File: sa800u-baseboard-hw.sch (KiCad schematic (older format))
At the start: 4 parts

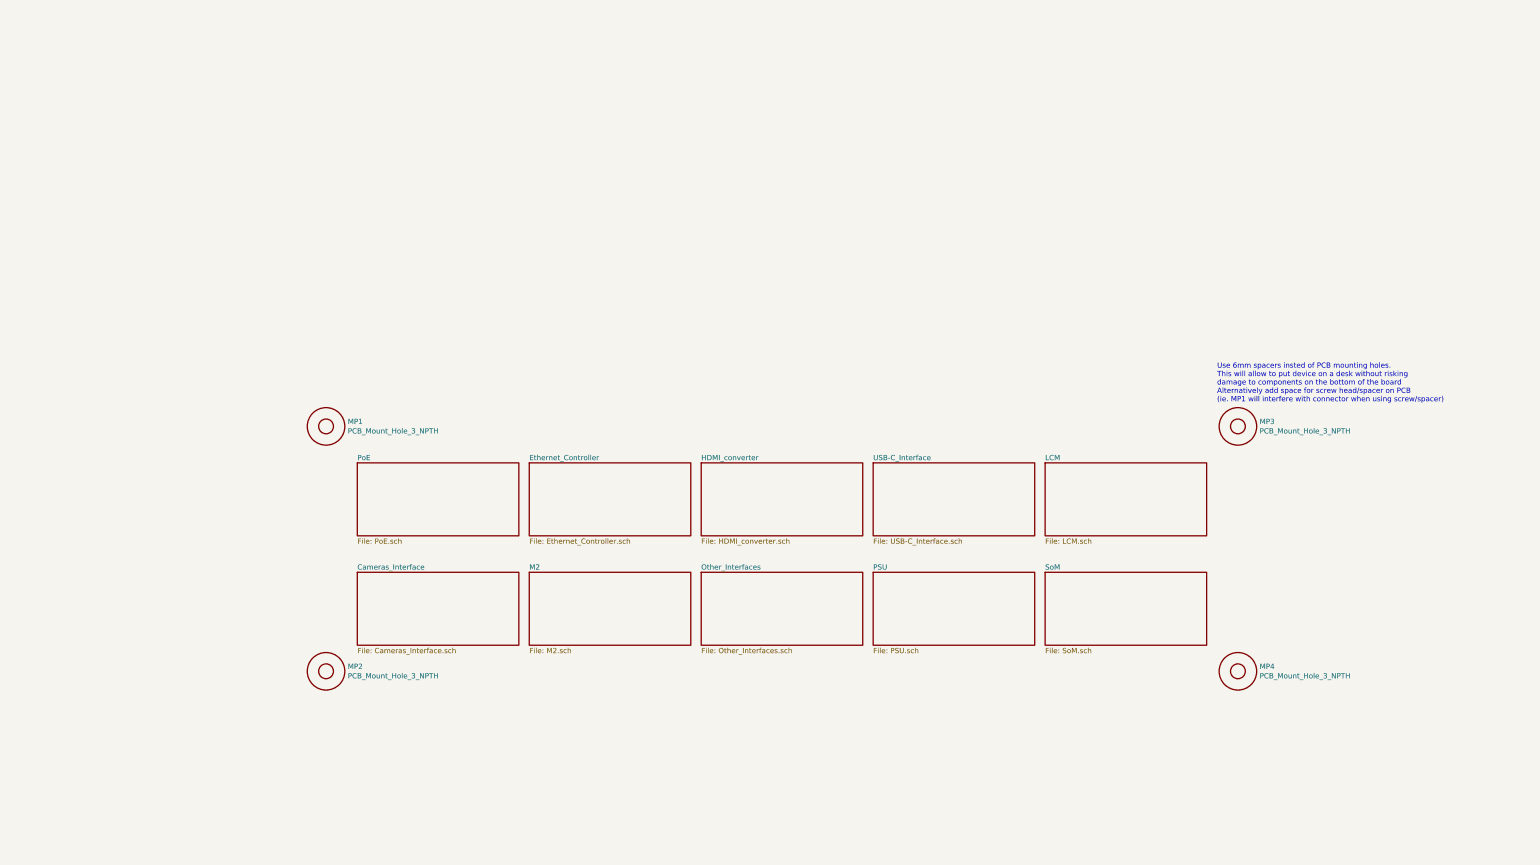
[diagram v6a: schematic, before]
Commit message: changed mounting holes to spacers
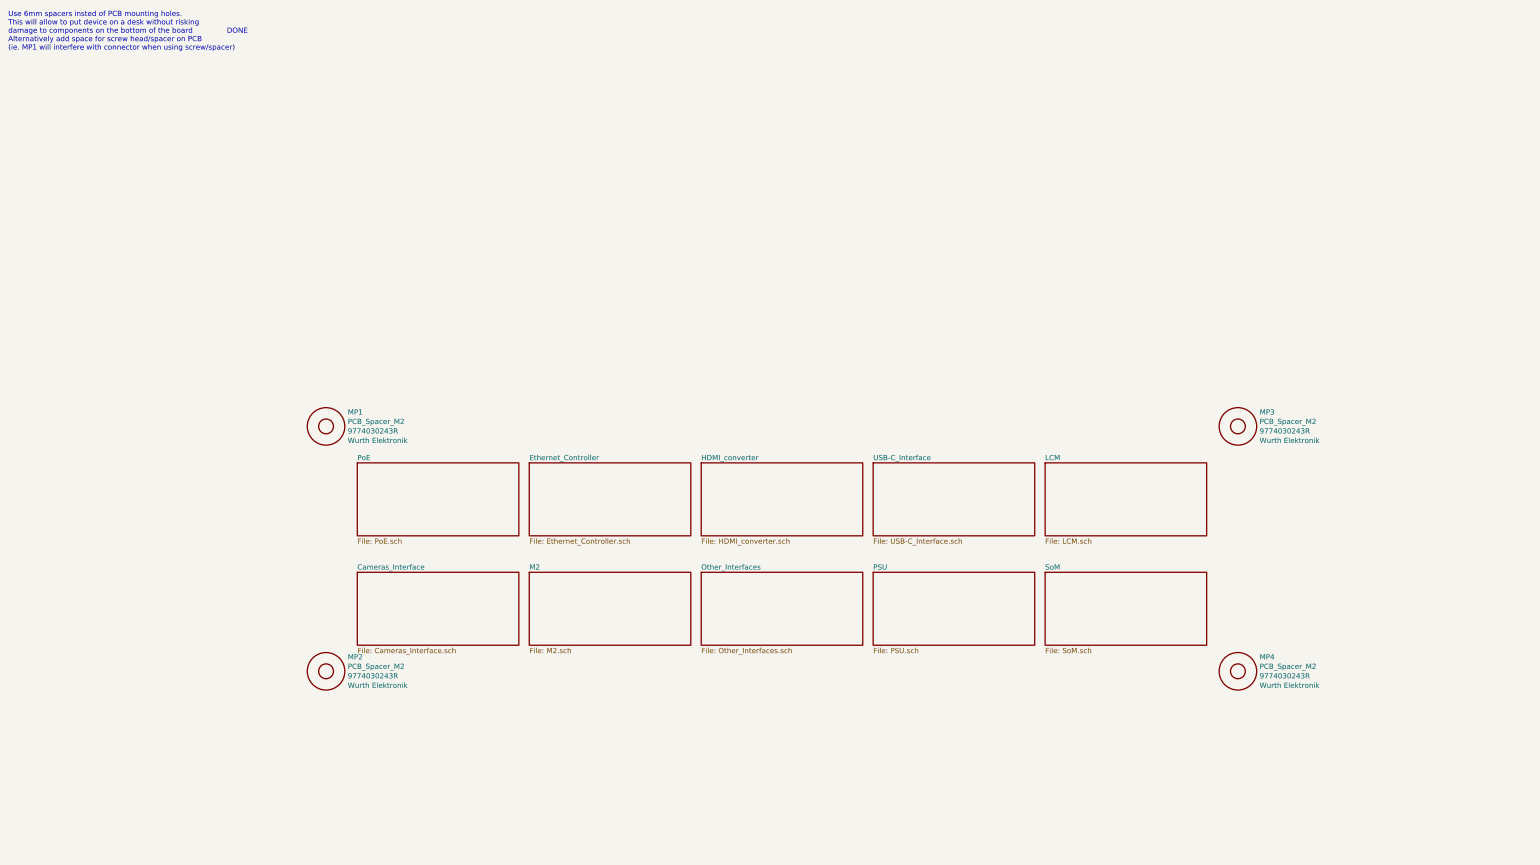
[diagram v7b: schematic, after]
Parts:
- removed MP1, MP2, MP3, MP4: PCB_Mount_Hole_3_NPTH, sa800u-baseboard-hw-footprints:mounting-hole-3mm-NPTH, symbol sa800u-baseboard-hw:PCB_Mount_Hole_3_NPTH
- added MP1, MP2, MP3, MP4: PCB_Spacer_M2, antmicro-footprints:9774030243R, symbol antmicroMechanicalParts:PCB_Spacer_M2
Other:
- note added: "Use 6mm spacers insted of PCB mounting holes.\nThis will allow to put device on a desk without risking \ndamage to components on the bottom of the board DONE\nAlternatively add space for screw head/spacer on PCB\n(ie. MP1 will interfere with connector when using screw/spacer)"
- note removed: "Use 6mm spacers insted of PCB mounting holes.\nThis will allow to put device on a desk without risking \ndamage to components on the bottom of the board \nAlternatively add space for screw head/spacer on PCB\n(ie. MP1 will interfere with connector when using screw/spacer)"
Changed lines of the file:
@@
 F1 "PSU.sch" 50
 $EndSheet
-$Comp
-L sa800u-baseboard-hw:PCB_Mount_Hole_3_NPTH MP1
-U 1 1 61B52107
-P 3550 4500
-F 0 "MP1" H 3758 4546 50  0000 L CNN
-F 1 "PCB_Mount_Hole_3_NPTH" H 3758 4455 50  0000 L CNN
-F 2 "sa800u-baseboard-hw-footprints:mounting-hole-3mm-NPTH" H 4350 5200 50  0001 C CNN
-F 3 "" H 4500 5300 50  0001 C CNN
-	1    3550 4500
-	1    0    0    -1
-$EndComp
-$Comp
-L sa800u-baseboard-hw:PCB_Mount_Hole_3_NPTH MP3
-U 1 1 61B52579
-P 12300 4500
-F 0 "MP3" H 12508 4546 50  0000 L CNN
-F 1 "PCB_Mount_Hole_3_NPTH" H 12508 4455 50  0000 L CNN
-F 2 "sa800u-baseboard-hw-footprints:mounting-hole-3mm-NPTH" H 13100 5200 50  0001 C CNN
-F 3 "" H 13250 5300 50  0001 C CNN
-	1    12300 4500
-	1    0    0    -1
-$EndComp
-$Comp
-L sa800u-baseboard-hw:PCB_Mount_Hole_3_NPTH MP2
-U 1 1 61B52868
-P 3550 6850
-F 0 "MP2" H 3758 6896 50  0000 L CNN
-F 1 "PCB_Mount_Hole_3_NPTH" H 3758 6805 50  0000 L CNN
-F 2 "sa800u-baseboard-hw-footprints:mounting-hole-3mm-NPTH" H 4350 7550 50  0001 C CNN
-F 3 "" H 4500 7650 50  0001 C CNN
-	1    3550 6850
-	1    0    0    -1
-$EndComp
-$Comp
-L sa800u-baseboard-hw:PCB_Mount_Hole_3_NPTH MP4
-U 1 1 61B52B11
-P 12300 6850
-F 0 "MP4" H 12508 6896 50  0000 L CNN
-F 1 "PCB_Mount_Hole_3_NPTH" H 12508 6805 50  0000 L CNN
-F 2 "sa800u-baseboard-hw-footprints:mounting-hole-3mm-NPTH" H 13100 7550 50  0001 C CNN
-F 3 "" H 13250 7650 50  0001 C CNN
-	1    12300 6850
-	1    0    0    -1
-$EndComp
 $Sheet
 S 3850 4850 1550 700
@@
 F1 "PoE.sch" 50
 $EndSheet
-Text Notes 12100 4275 0    50   ~ 0
-Use 6mm spacers insted of PCB mounting holes.\nThis will allow to put device on a desk without risking \ndamage to components on the bottom of the board \nAlternatively add space for screw head/spacer on PCB\n(ie. MP1 will interfere with connector when using screw/spacer)
+$Comp
+L antmicroMechanicalParts:PCB_Spacer_M2 MP3
+U 1 1 61E50FA3
+P 12300 4500
+F 0 "MP3" H 12508 4637 50  0000 L CNN
+F 1 "PCB_Spacer_M2" H 12508 4546 50  0000 L CNN
+F 2 "antmicro-footprints:9774030243R" H 13100 5200 50  0001 C CNN
+F 3 "https://katalog.we-online.de/em/datasheet/9774030243R.pdf" H 13250 5300 50  0001 C CNN
+F 4 "9774030243R" H 12508 4455 50  0000 L CNN "MPN"
+F 5 "Wurth Elektronik " H 12508 4364 50  0000 L CNN "Manufacturer"
+	1    12300 4500
+	1    0    0    -1
+$EndComp
+$Comp
+L antmicroMechanicalParts:PCB_Spacer_M2 MP4
+U 1 1 61E5197E
+P 12300 6850
+F 0 "MP4" H 12508 6987 50  0000 L CNN
+F 1 "PCB_Spacer_M2" H 12508 6896 50  0000 L CNN
+F 2 "antmicro-footprints:9774030243R" H 13100 7550 50  0001 C CNN
+F 3 "https://katalog.we-online.de/em/datasheet/9774030243R.pdf" H 13250 7650 50  0001 C CNN
+F 4 "9774030243R" H 12508 6805 50  0000 L CNN "MPN"
+F 5 "Wurth Elektronik " H 12508 6714 50  0000 L CNN "Manufacturer"
+	1    12300 6850
+	1    0    0    -1
+$EndComp
+$Comp
+L antmicroMechanicalParts:PCB_Spacer_M2 MP2
+U 1 1 61E52039
+P 3550 6850
+F 0 "MP2" H 3758 6987 50  0000 L CNN
+F 1 "PCB_Spacer_M2" H 3758 6896 50  0000 L CNN
+F 2 "antmicro-footprints:9774030243R" H 4350 7550 50  0001 C CNN
+F 3 "https://katalog.we-online.de/em/datasheet/9774030243R.pdf" H 4500 7650 50  0001 C CNN
+F 4 "9774030243R" H 3758 6805 50  0000 L CNN "MPN"
+F 5 "Wurth Elektronik " H 3758 6714 50  0000 L CNN "Manufacturer"
+	1    3550 6850
+	1    0    0    -1
+$EndComp
+$Comp
+L antmicroMechanicalParts:PCB_Spacer_M2 MP1
+U 1 1 61E52603
+P 3550 4500
+F 0 "MP1" H 3758 4637 50  0000 L CNN
+F 1 "PCB_Spacer_M2" H 3758 4546 50  0000 L CNN
+F 2 "antmicro-footprints:9774030243R" H 4350 5200 50  0001 C CNN
+F 3 "https://katalog.we-online.de/em/datasheet/9774030243R.pdf" H 4500 5300 50  0001 C CNN
+F 4 "9774030243R" H 3758 4455 50  0000 L CNN "MPN"
+F 5 "Wurth Elektronik " H 3758 4364 50  0000 L CNN "Manufacturer"
+	1    3550 4500
+	1    0    0    -1
+$EndComp
+Text Notes 500  900  0    50   ~ 0
+Use 6mm spacers insted of PCB mounting holes.\nThis will allow to put device on a desk without risking \ndamage to components on the bottom of the board               DONE\nAlternatively add space for screw head/spacer on PCB\n(ie. MP1 will interfere with connector when using screw/spacer)
 $EndSCHEMATC

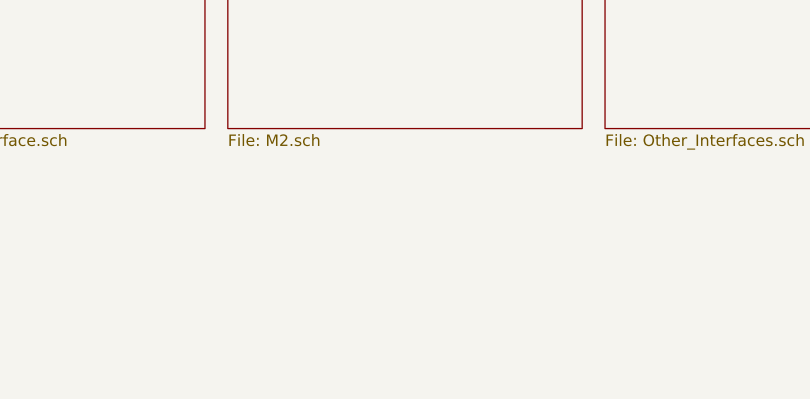
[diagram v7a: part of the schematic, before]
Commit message: add temp psu sheet
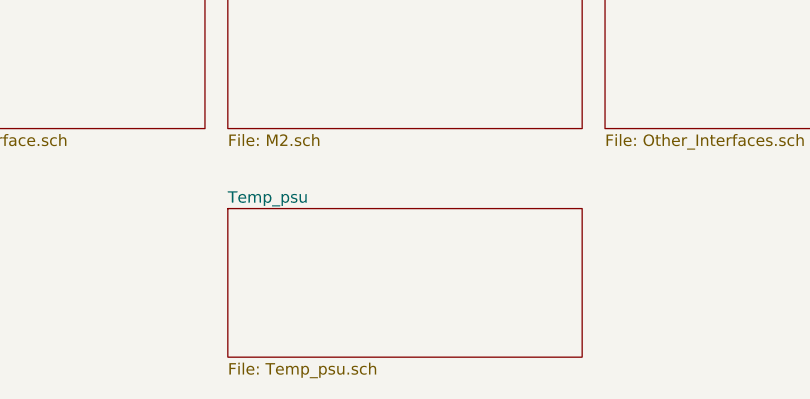
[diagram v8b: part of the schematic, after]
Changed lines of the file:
@@
 $Descr A3 16535 11693
 encoding utf-8
-Sheet 1 11
+Sheet 1 12
 Title ""
 Date ""
@@
 Text Notes 500  900  0    50   ~ 0
 Use 6mm spacers insted of PCB mounting holes.\nThis will allow to put device on a desk without risking \ndamage to components on the bottom of the board               DONE\nAlternatively add space for screw head/spacer on PCB\n(ie. MP1 will interfere with connector when using screw/spacer)
+$Sheet
+S 5500 6950 1550 650
+U 61DC2BE0
+F0 "Temp_psu" 50
+F1 "Temp_psu.sch" 50
+$EndSheet
 $EndSCHEMATC
